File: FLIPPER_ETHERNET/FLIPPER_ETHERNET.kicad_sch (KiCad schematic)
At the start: 26 parts, among them J1 RJ45_Hanrun_HR911105A_Horizon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, J2 Conn_01x08_Socket, J3 Conn_01x10_Socket, SW1 SW_Push, U1 ENC28J60x-ML, Y1 25MHz

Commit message: feat: bom added
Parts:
- SW1: #LSCS C318889 -> C2886897
- Y1: #LSCS (none) -> C390792; Proveedor (none) -> LCSC; manf# (none) -> S2125000101080
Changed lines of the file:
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@@
+			)
+		)
+		(property "#LSCS" "C390792"
+			(at 38.1 123.19 0)
+			(effects
+				(font
+					(size 1.27 1.27)
+				)
+				(hide yes)
+			)
+		)
+		(property "Proveedor" "LCSC"
+			(at 38.1 123.19 0)
+			(effects
+				(font
+					(size 1.27 1.27)
+				)
+				(hide yes)
+			)
+		)
+		(property "manf#" " S2125000101080"
+			(at 38.1 123.19 0)
+			(effects
+				(font
+					(size 1.27 1.27)
+				)
+				(hide yes)
 			)
 		)
@@
 			)
 		)
-		(property "#LSCS" " C318889"
+		(property "#LSCS" "C2886897"
 			(at 44.45 64.77 0)
 			(effects

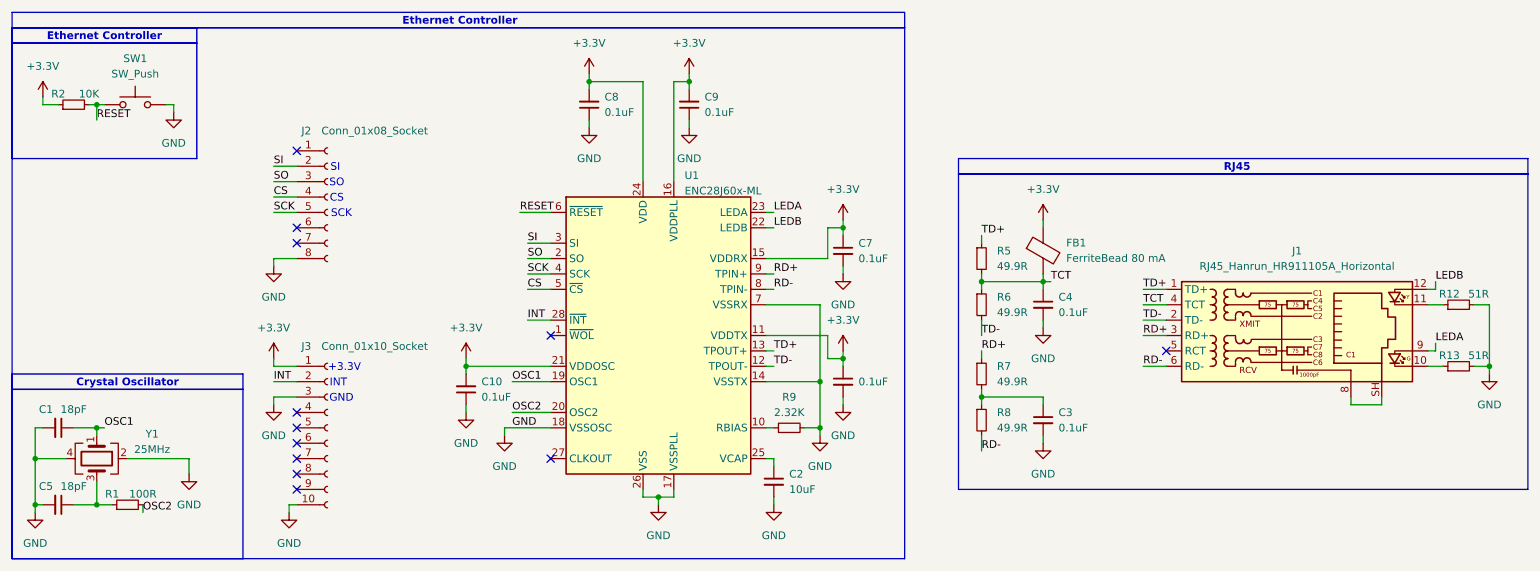
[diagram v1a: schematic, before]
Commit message: feat: Y1 updated in flipper ethernet bom
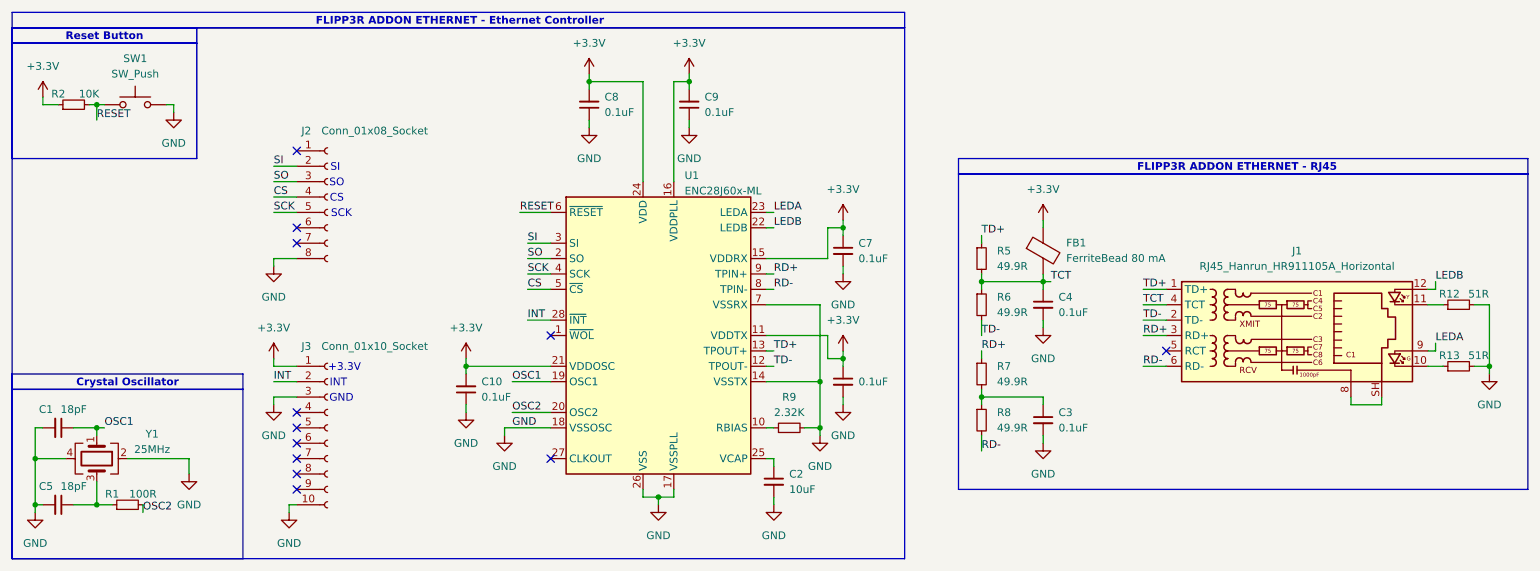
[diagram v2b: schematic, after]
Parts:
- J1: #LSCS C85824 -> C12074
- J2: #LSCS C7501586 -> C7501586
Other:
- note added: "FLIPP3R ADDON ETHERNET - Ethernet Controller"
- note added: "FLIPP3R ADDON ETHERNET - RJ45"
- note added: "Reset Button"
- note removed: "Ethernet Controller"
- note removed: "RJ45"
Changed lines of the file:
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@@
 		)
 	)
-	(text "Ethernet Controller"
+	(text "FLIPP3R ADDON ETHERNET - Ethernet Controller"
 		(exclude_from_sim no)
 		(at 98.044 51.054 0)
@@
 		)
 	)
-	(text "RJ45"
+	(text "FLIPP3R ADDON ETHERNET - RJ45"
 		(exclude_from_sim no)
 		(at 226.314 75.184 0)
@@
 		)
 	)
-	(text "Ethernet Controller"
+	(text "Reset Button"
 		(exclude_from_sim no)
 		(at 39.37 53.594 0)
@@
 			)
 		)
-		(property "Datasheet" "~"
+		(property "Datasheet" "https://www.lcsc.com/datasheet/lcsc_datasheet_2304140030_JGHC-S2125000101080_C390792.pdf"
 			(at 38.1 123.19 0)
 			(effects
@@
 			)
 		)
-		(property "#LSCS" "C85824"
+		(property "#LSCS" "C12074"
 			(at 234.95 102.87 0)
 			(effects
@@
 			)
 		)
-		(property "Datasheet" "~"
+		(property "Datasheet" "https://www.lcsc.com/datasheet/lcsc_datasheet_2312131724_Vishay-Intertech-ILBB0805ER202V_C6639322.pdf"
 			(at 194.31 88.9 0)
 			(effects
@@
 			)
 		)
-		(property "#LSCS" " C7501586"
+		(property "#LSCS" "C7501586"
 			(at 76.2 80.01 0)
 			(effects

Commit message: feat(Hw): changed reset to flipper
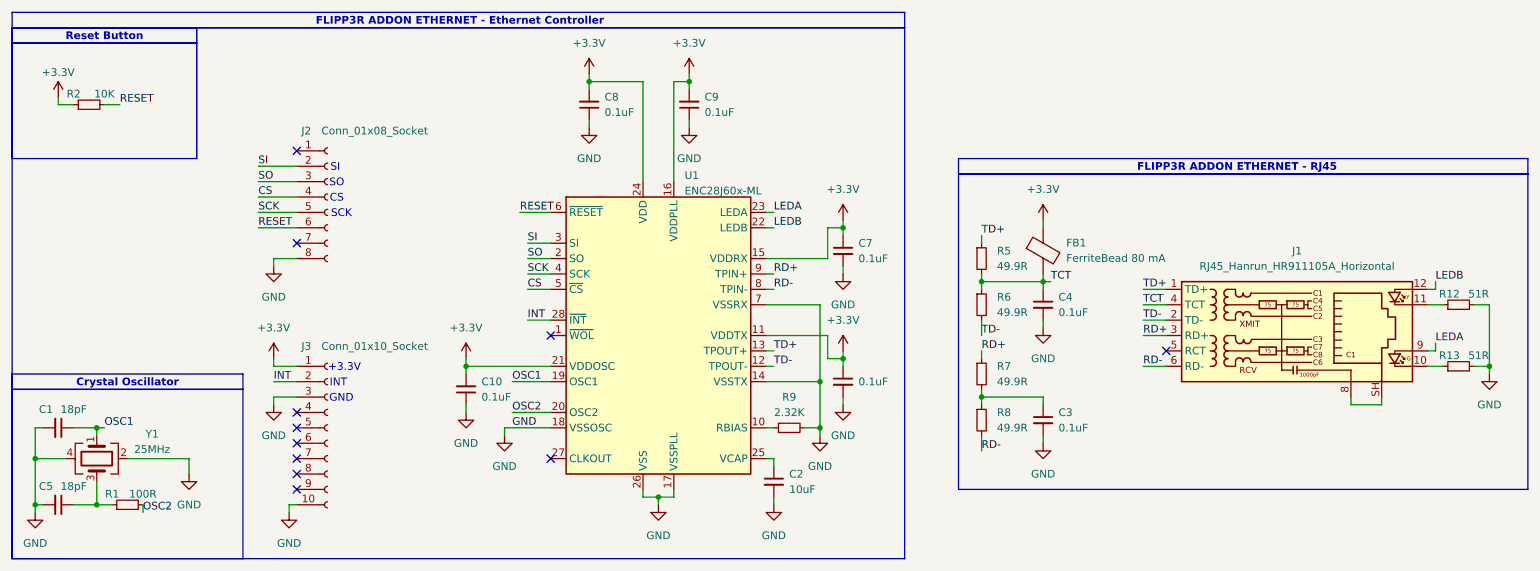
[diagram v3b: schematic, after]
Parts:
- removed SW1: SW_Push, Button_Switch_SMD:SW_Push_1P1T_XKB_TS-1187A, symbol Switch:SW_Push
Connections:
- net RESET: now also J2.6 (Pin_6)
- no-connect marks 12 -> 11
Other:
- moved on the sheet: R2

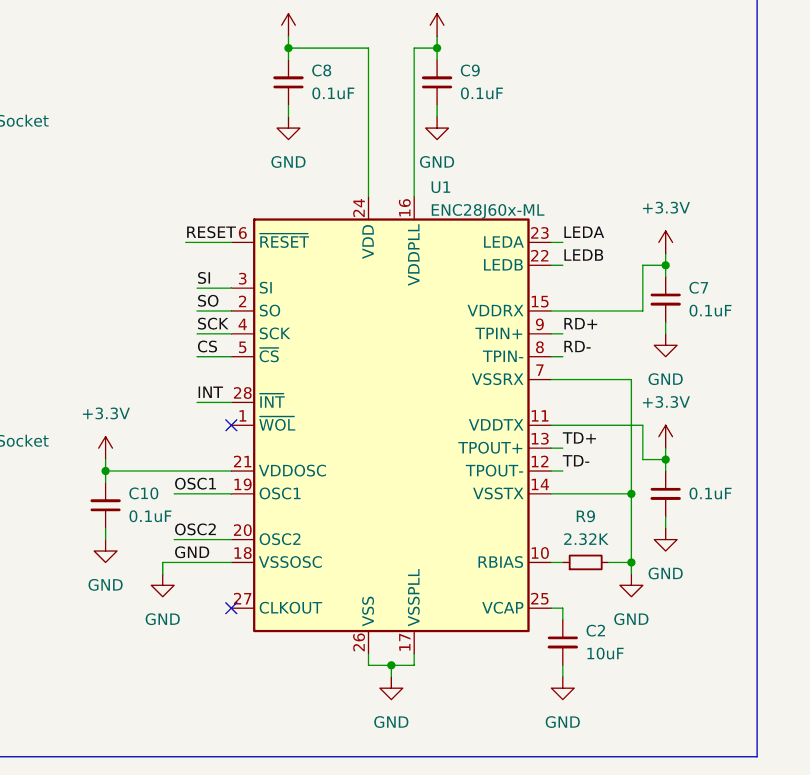
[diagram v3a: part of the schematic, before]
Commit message: refactor(hw): move components
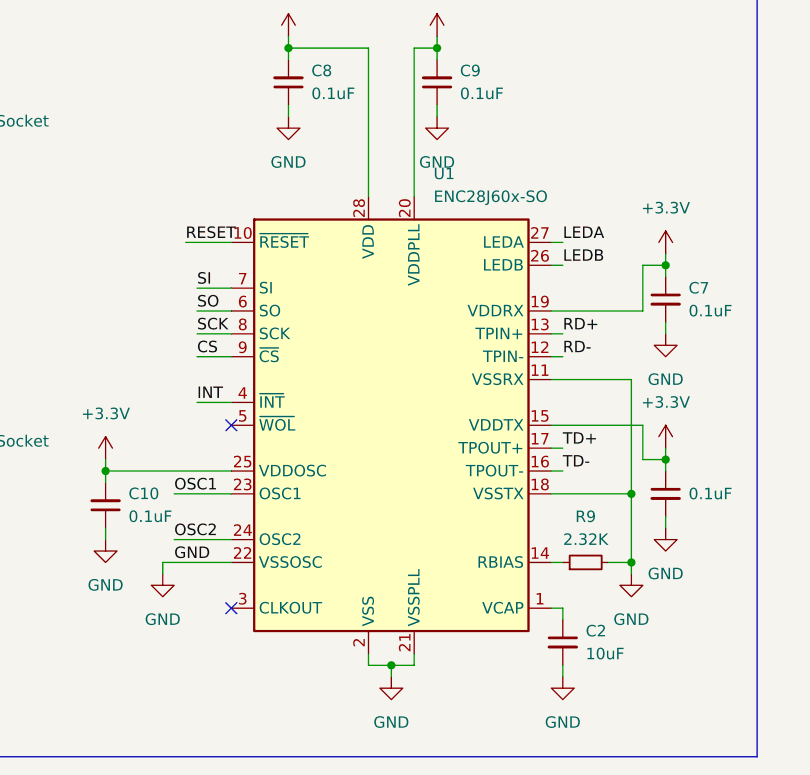
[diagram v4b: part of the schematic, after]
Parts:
- removed U1: ENC28J60x-ML, Package_DFN_QFN:QFN-28-1EP_6x6mm_P0.65mm_EP4.25x4.25mm, symbol Interface_Ethernet:ENC28J60x-ML
- added U1: ENC28J60x-SO, Package_SO:SOIC-28W_7.5x17.9mm_P1.27mm, symbol Interface_Ethernet:ENC28J60x-SO
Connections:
- net +3.3V: now also U1.15 (VDDTX), U1.19 (VDDRX), U1.20 (VDDPLL), U1.25 (VDDOSC), U1.28 (VDD)
- net CS: now also U1.9 (~{CS})
- net GND: now also U1.11 (VSSRX), U1.18 (VSSTX), U1.2 (VSS), U1.21 (VSSPLL), U1.22 (VSSOSC)
- net INT: now also U1.4 (~{INT})
- net LEDA: now also U1.27 (LEDA)
- net LEDB: now also U1.26 (LEDB)
- net OSC1: now also U1.23 (OSC1)
- net OSC2: now also U1.24 (OSC2)
- net RD+: now also U1.13 (TPIN+)
- net RD-: now also U1.12 (TPIN-)
- net RESET: now also U1.10 (~{RESET})
- net SCK: now also U1.8 (SCK)
- net SI: now also U1.7 (SI)
- net SO: now also U1.6 (SO)
- net TD+: now also U1.17 (TPOUT+)
- net TD-: now also U1.16 (TPOUT-)
- net at R9.1: now also U1.14 (RBIAS)
- net at C2.1: now also U1.1 (VCAP)
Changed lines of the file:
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@@
 	)
 	(symbol
-		(lib_id "Interface_Ethernet:ENC28J60x-ML")
+		(lib_id "Interface_Ethernet:ENC28J60x-SO")
 		(at 130.81 102.87 0)
 		(unit 1)
@@
 		(on_board yes)
 		(dnp no)
+		(fields_autoplaced yes)
 		(property "Reference" "U1"
-			(at 135.128 76.454 0)
+			(at 135.4933 74.93 0)
 			(effects
 				(font
@@
 			)
 		)
-		(property "Value" "ENC28J60x-ML"
-			(at 135.128 78.994 0)
+		(property "Value" "ENC28J60x-SO"
+			(at 135.4933 77.47 0)
 			(effects
 				(font
@@
 			)
 		)
-		(property "Footprint" "Package_DFN_QFN:QFN-28-1EP_6x6mm_P0.65mm_EP4.25x4.25mm"
-			(at 161.29 127 0)
+		(property "Footprint" "Package_SO:SOIC-28W_7.5x17.9mm_P1.27mm"
+			(at 160.02 127 0)
 			(effects
 				(font
@@
 			)
 		)
-		(property "Datasheet" "https://ww1.microchip.com/downloads/aemDocuments/documents/OTH/ProductDocuments/DataSheets/39662e.pdf"
+		(property "Datasheet" "http://ww1.microchip.com/downloads/en/devicedoc/39662e.pdf"
 			(at 130.81 102.87 0)
 			(effects
@@
 			)
 		)
-		(property "Description" "ENC28J60 Single Chip Ethernet Interface,QFN-28"
+		(property "Description" "ENC28J60 Single Chip Ethernet Interface, SOIC-28"
 			(at 130.81 102.87 0)
 			(effects
@@
 			)
 		)
-		(property "#LSCS" "C57281"
-			(at 130.81 102.87 0)
-			(effects
-				(font
-					(size 1.27 1.27)
-				)
-				(hide yes)
-			)
+		(pin "11"
 		)
-		(property "Arrow Part Number" ""
-			(at 130.81 102.87 0)
-			(effects
-				(font
-					(size 1.27 1.27)
-				)
-				(hide yes)
-			)
-		)
-		(property "Arrow Price/Stock" ""
-			(at 130.81 102.87 0)
-			(effects
-				(font
-					(size 1.27 1.27)
-				)
-				(hide yes)
-			)
-		)
-		(property "Height" ""
-			(at 130.81 102.87 0)
-			(effects
-				(font
-					(size 1.27 1.27)
-				)
-				(hide yes)
-			)
-		)
-		(property "Manufacturer_Name" ""
-			(at 130.81 102.87 0)
-			(effects
-				(font
-					(size 1.27 1.27)
-				)
-				(hide yes)
-			)
-		)
-		(property "Manufacturer_Part_Number" ""
-			(at 130.81 102.87 0)
-			(effects
-				(font
-					(size 1.27 1.27)
-				)
-				(hide yes)
-			)
-		)
-		(property "Mouser Part Number" ""
-			(at 130.81 102.87 0)
-			(effects
-				(font
-					(size 1.27 1.27)
-				)
-				(hide yes)
-			)
-		)
-		(property "Mouser Price/Stock" ""
-			(at 130.81 102.87 0)
-			(effects
-				(font
-					(size 1.27 1.27)
-				)
-				(hide yes)
-			)
-		)
-		(property "Proveedor" "Mouser"
-			(at 130.81 102.87 0)
-			(effects
-				(font
-					(size 1.27 1.27)
-				)
-				(hide yes)
-			)
-		)
-		(property "manf#" "ENC28J60-I/ML"
-			(at 130.81 102.87 0)
-			(effects
-				(font
-					(size 1.27 1.27)
-				)
-				(hide yes)
-			)
-		)
-		(pin "14"
-		)
-		(pin "12"
-		)
-		(pin "3"
-		)
-		(pin "10"
+		(pin "19"
 		)
 		(pin "24"
 		)
-		(pin "11"
+		(pin "26"
 		)
-		(pin "28"
+		(pin "18"
+		)
+		(pin "2"
 		)
 		(pin "22"
 		)
-		(pin "7"
+		(pin "25"
+		)
+		(pin "15"
 		)
 		(pin "17"
@@
 		(pin "23"
 		)
-		(pin "5"
-		)
-		(pin "16"
-		)
-		(pin "21"
-		)
-		(pin "26"
-		)
-		(pin "9"
-		)
-		(pin "15"
-		)
-		(pin "4"
-		)
-		(pin "19"
-		)
-		(pin "2"
+		(pin "14"
 		)
 		(pin "1"
 		)
-		(pin "25"
+		(pin "13"
 		)
-		(pin "13"
+		(pin "21"
 		)
 		(pin "27"
@@
 		(pin "20"
 		)
+		(pin "12"
+		)
+		(pin "28"
+		)
+		(pin "16"
+		)
+		(pin "3"
+		)
+		(pin "7"
+		)
 		(pin "8"
 		)
-		(pin "18"
+		(pin "10"
+		)
+		(pin "4"
+		)
+		(pin "9"
 		)
 		(pin "6"
 		)
+		(pin "5"
+		)
 		(instances

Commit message: feat(hw): add routes
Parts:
- C1, C10, C2, C3, C4, C5, C6, C7, C8, C9, FB1, J1, J2, J3, R12, R13, R2, R5, R6, R7, R8, R9, Y1: Proveedor LCSC -> JLCPCB
- R1: Proveedor LCSC -> JLCPBC
- U1: #LSCS (none) -> C47351; Proveedor (none) -> JLCPCB
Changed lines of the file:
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@@
 			)
 		)
-		(property "Proveedor" "LCSC"
+		(property "Proveedor" "JLCPCB"
 			(at 184.15 109.22 0)
 			(effects
@@
 			)
 		)
-		(property "Proveedor" "LCSC"
+		(property "Proveedor" "JLCPCB"
 			(at 36.83 64.77 0)
 			(effects
@@
 			)
 		)
-		(property "Proveedor" "LCSC"
+		(property "Proveedor" "JLCPCB"
 			(at 194.31 116.84 0)
 			(effects
@@
 			)
 		)
-		(property "Proveedor" "LCSC"
+		(property "Proveedor" "JLCPCB"
 			(at 119.38 64.77 0)
 			(effects
@@
 			)
 		)
-		(property "Proveedor" "LCSC"
+		(property "Proveedor" "JLCPCB"
 			(at 38.1 123.19 0)
 			(effects
@@
 			)
 		)
-		(property "Proveedor" "LCSC"
+		(property "Proveedor" "JLCPCB"
 			(at 234.95 102.87 0)
 			(effects
@@
 			)
 		)
-		(property "Proveedor" "LCSC"
+		(property "Proveedor" "JLCPCB"
 			(at 31.75 130.81 0)
 			(effects
@@
 			)
 		)
-		(property "Proveedor" "LCSC"
+		(property "Proveedor" "JLCPCB"
 			(at 76.2 118.11 0)
 			(effects
@@
 			)
 		)
-		(property "Proveedor" "LCSC"
+		(property "Proveedor" "JLCPCB"
 			(at 184.15 90.17 0)
 			(effects
@@
 			)
 		)
-		(property "Proveedor" "LCSC"
+		(property "Proveedor" "JLCPCB"
 			(at 152.4 118.11 0)
 			(effects
@@
 			)
 		)
-		(property "Proveedor" "LCSC"
+		(property "Proveedor" "JLCPCB"
 			(at 184.15 97.79 0)
 			(effects
@@
 			)
 		)
+		(property "Proveedor" "JLCPCB"
+			(at 130.81 102.87 0)
+			(effects
+				(font
+					(size 1.27 1.27)
+				)
+				(hide yes)
+			)
+		)
+		(property "#LSCS" "C47351"
+			(at 130.81 102.87 0)
+			(effects
+				(font
+					(size 1.27 1.27)
+				)
+				(hide yes)
+			)
+		)
 		(pin "11"
 		)
@@
 			)
 		)
-		(property "Proveedor" "LCSC"
+		(property "Proveedor" "JLCPCB"
 			(at 99.06 111.76 0)
 			(effects
@@
 			)
 		)
-		(property "Proveedor" "LCSC"
+		(property "Proveedor" "JLCPCB"
 			(at 135.89 64.77 0)
 			(effects
@@
 			)
 		)
-		(property "Proveedor" "LCSC"
+		(property "Proveedor" "JLCPCB"
 			(at 194.31 88.9 0)
 			(effects
@@
 			)
 		)
-		(property "Proveedor" "LCSC"
+		(property "Proveedor" "JLCPCB"
 			(at 194.31 97.79 0)
 			(effects
@@
 			)
 		)
-		(property "Proveedor" "LCSC"
+		(property "Proveedor" "JLCPCB"
 			(at 262.89 107.95 0)
 			(effects
@@
 			)
 		)
-		(property "Proveedor" "LCSC"
+		(property "Proveedor" "JLCPCB"
 			(at 262.89 97.79 0)
 			(effects
@@
 			)
 		)
-		(property "Proveedor" "LCSC"
+		(property "Proveedor" "JLCPCB"
 			(at 184.15 116.84 0)
 			(effects
@@
 			)
 		)
-		(property "Proveedor" "LCSC"
+		(property "Proveedor" "JLCPBC"
 			(at 43.18 130.81 0)
 			(effects
@@
 			)
 		)
-		(property "Proveedor" "LCSC"
+		(property "Proveedor" "JLCPCB"
 			(at 149.86 127 0)
 			(effects
@@
 			)
 		)
-		(property "Proveedor" "LCSC"
+		(property "Proveedor" "JLCPCB"
 			(at 161.29 88.9 0)
 			(effects
@@
 			)
 		)
-		(property "Proveedor" "LCSC"
+		(property "Proveedor" "JLCPCB"
 			(at 31.75 118.11 0)
 			(effects
@@
 			)
 		)
-		(property "Proveedor" "LCSC"
+		(property "Proveedor" "JLCPCB"
 			(at 161.29 110.49 0)
 			(effects
@@
 			)
 		)
-		(property "Proveedor" "LCSC"
+		(property "Proveedor" "JLCPCB"
 			(at 76.2 80.01 0)
 			(effects
